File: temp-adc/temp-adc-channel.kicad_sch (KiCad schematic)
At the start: 4 parts

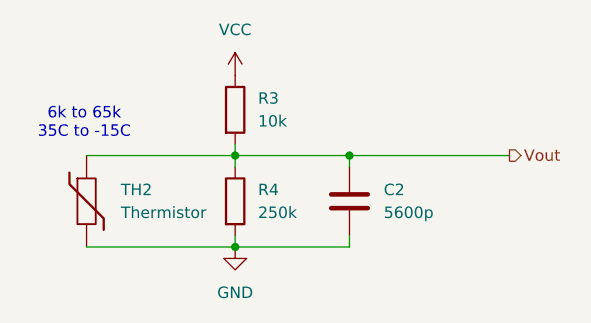
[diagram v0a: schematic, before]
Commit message: Created i2c adc project and schematic
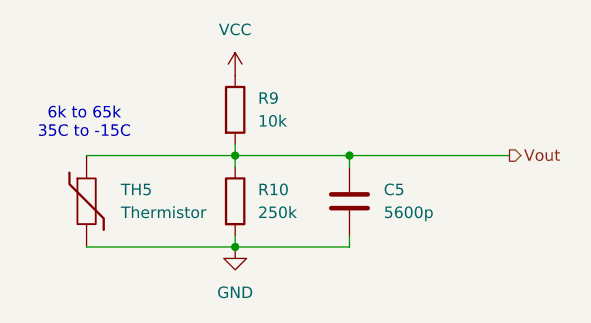
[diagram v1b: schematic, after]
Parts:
- renumbered C2 to C5, R4 to R10, R3 to R9, TH2 to TH5
